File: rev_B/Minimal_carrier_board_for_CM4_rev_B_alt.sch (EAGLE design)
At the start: 23 parts, among them IC1 MC74VHC1G14DFT1G, J1 P1-100, J2 P101-200, J5 HRO_31_M_12_USB_C, J6 629104190121, J7 SFW15R-2STE1LF

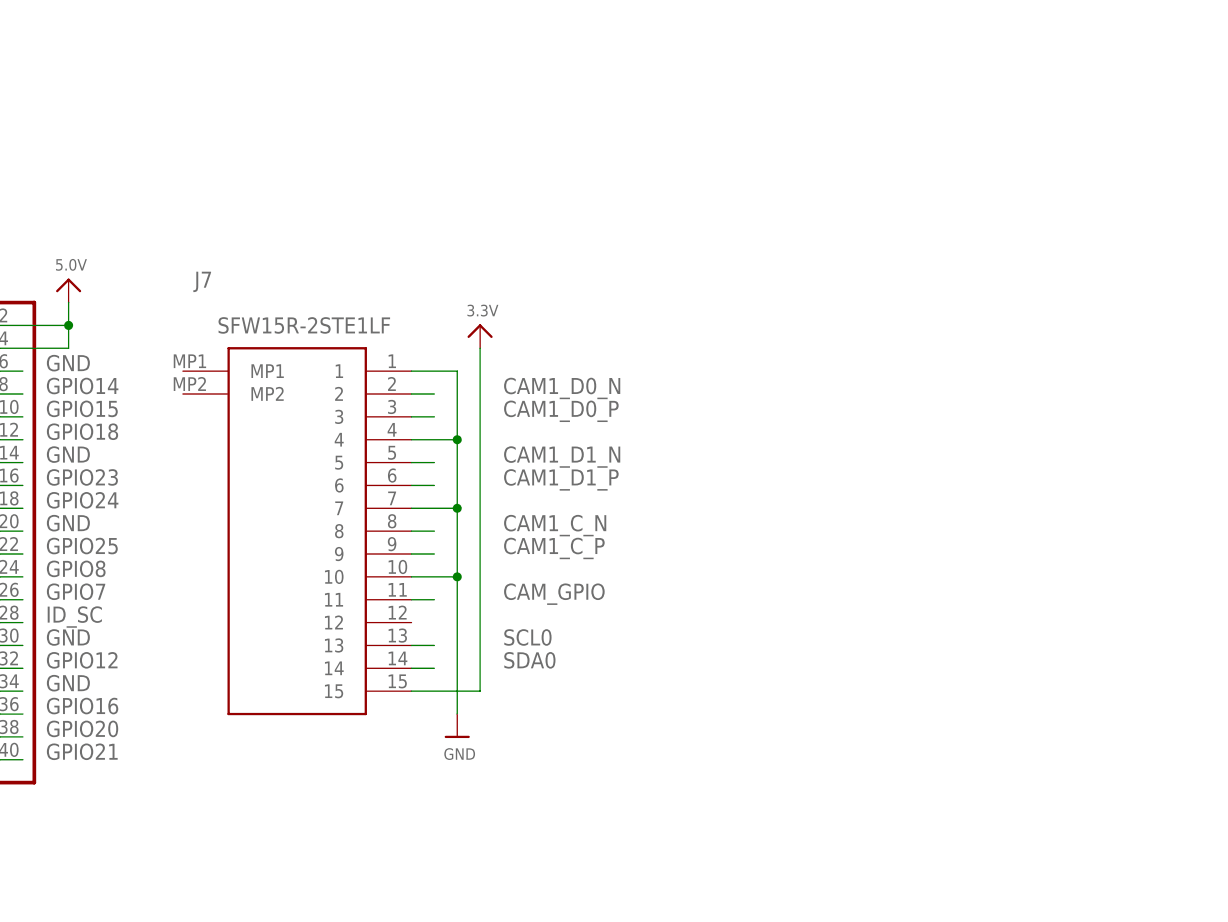
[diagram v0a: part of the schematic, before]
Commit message: Update
- renamed files so there are now 2 versions of rev.B:

rev.B now have 15-pin connector for RPi camera  module
rev.B_alt have 22-pin connector for RPi camera module and DSI display
- added/updated pictures for both versions of the board
- updated README accordingly
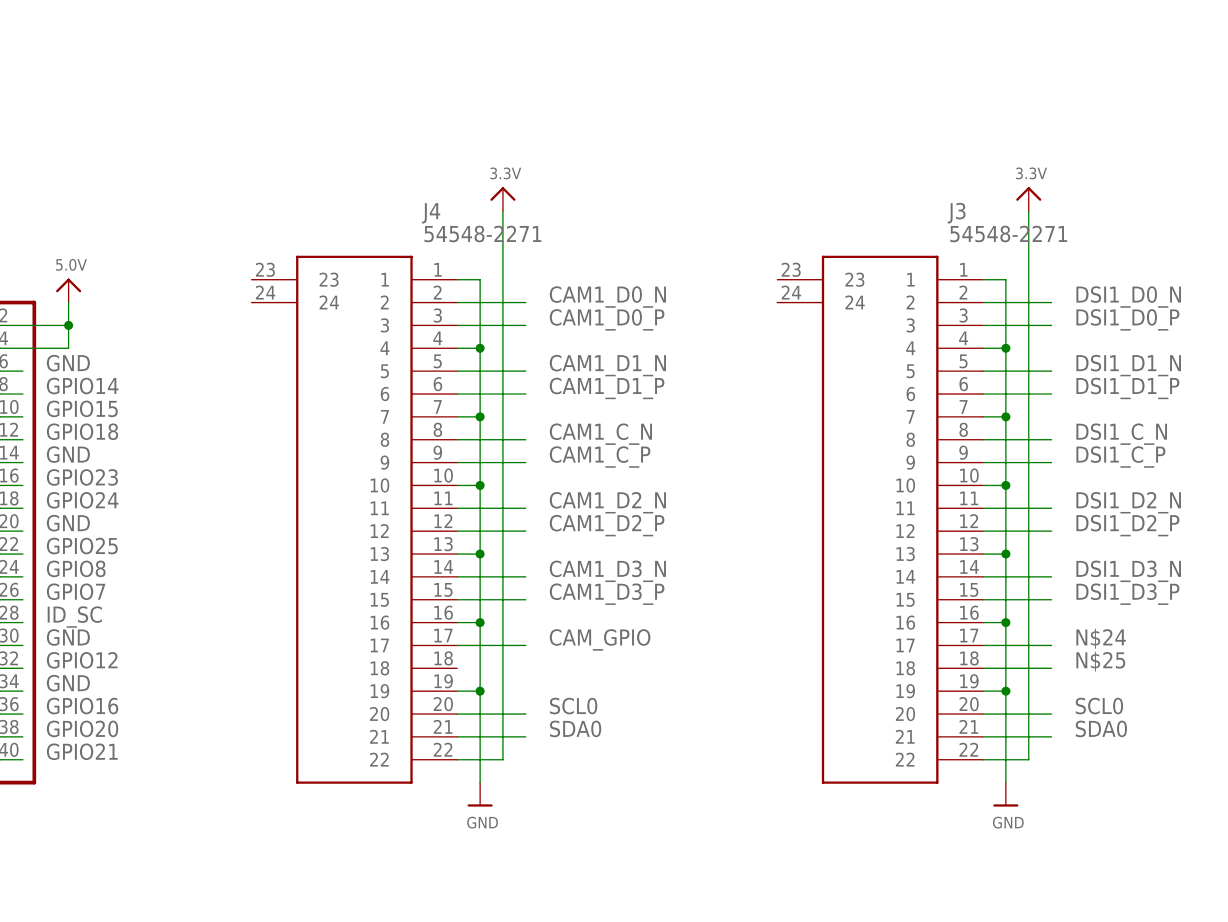
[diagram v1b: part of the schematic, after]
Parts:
- removed J7: SFW15R-2STE1LF, SamacSys_Parts:SFW15R-2STE1LF
- added J3, J4: 54548-2271, dronecz:54548-2271
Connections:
- new net N$24: J3.17
- new net N$25: J3.18
- net 3.3V: now also J3.22, J4.22; no longer J7.15
- net CAM1_C_N: now also J4.8; no longer J7.8
- net CAM1_C_P: now also J4.9; no longer J7.9
- net CAM1_D0_N: now also J4.2; no longer J7.2
- net CAM1_D0_P: now also J4.3; no longer J7.3
- net CAM1_D1_N: now also J4.5; no longer J7.5
- net CAM1_D1_P: now also J4.6; no longer J7.6
- net CAM1_D2_N: now also J4.11
- net CAM1_D2_P: now also J4.12
- net CAM1_D3_N: now also J4.14
- net CAM1_D3_P: now also J4.15
- net CAM_GPIO: now also J4.17; no longer J7.11
- net DSI1_C_N: now also J3.8
- net DSI1_C_P: now also J3.9
- net DSI1_D0_N: now also J3.2
- net DSI1_D0_P: now also J3.3
- net DSI1_D1_N: now also J3.5
- net DSI1_D1_P: now also J3.6
- net DSI1_D2_N: now also J3.11
- net DSI1_D2_P: now also J3.12
- net DSI1_D3_N: now also J3.14
- net DSI1_D3_P: now also J3.15
- net GND: now also J3.1, J3.10, J3.13, J3.16, J3.19, J3.4, J3.7, J4.1, J4.10, J4.13, J4.16, J4.19, J4.4, J4.7; no longer J7.1, J7.10, J7.4, J7.7
- net SCL0: now also J3.20, J4.20; no longer J7.13
- net SDA0: now also J3.21, J4.21; no longer J7.14
